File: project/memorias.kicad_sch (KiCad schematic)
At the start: 24 parts, among them U5 M93C66, U6 ICE40HX4K-TQ144, U7 W25X40CLSN

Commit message: Guardado previo, FTDI casi listo
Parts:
- renumbered C20 to C21, C21 to C22, C22 to C23, C23 to C24, C24 to C25
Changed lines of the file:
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@@
 		(on_board yes)
 		(dnp no)
-		(property "Reference" "#PWR038"
+		(property "Reference" "#PWR040"
 			(at 138.43 152.4 0)
 			(effects
@@
 			(project "fpga-utn"
 				(path "/fadb8841-cd7a-4174-937d-7c393e857c90/ddcff421-4d86-4360-8de5-a56571f2fa29"
-					(reference "#PWR038")
+					(reference "#PWR040")
 					(unit 1)
 				)
@@
 		(dnp no)
 		(fields_autoplaced yes)
-		(property "Reference" "#PWR027"
+		(property "Reference" "#PWR029"
 			(at 128.27 67.31 0)
 			(effects
@@
 			(project "fpga-utn"
 				(path "/fadb8841-cd7a-4174-937d-7c393e857c90/ddcff421-4d86-4360-8de5-a56571f2fa29"
-					(reference "#PWR027")
+					(reference "#PWR029")
 					(unit 1)
 				)
@@
 		(on_board yes)
 		(dnp no)
-		(property "Reference" "#PWR029"
+		(property "Reference" "#PWR031"
 			(at 162.56 100.33 0)
 			(effects
@@
 			(project "fpga-utn"
 				(path "/fadb8841-cd7a-4174-937d-7c393e857c90/ddcff421-4d86-4360-8de5-a56571f2fa29"
-					(reference "#PWR029")
+					(reference "#PWR031")
 					(unit 1)
 				)
@@
 		(on_board yes)
 		(dnp no)
-		(property "Reference" "C23"
+		(property "Reference" "C24"
 			(at 144.272 133.858 0)
 			(effects
@@
 			(project "fpga-utn"
 				(path "/fadb8841-cd7a-4174-937d-7c393e857c90/ddcff421-4d86-4360-8de5-a56571f2fa29"
-					(reference "C23")
+					(reference "C24")
 					(unit 1)
 				)
@@
 		(on_board yes)
 		(dnp no)
-		(property "Reference" "#PWR024"
+		(property "Reference" "#PWR026"
 			(at 115.57 55.88 0)
 			(effects
@@
 			(project "fpga-utn"
 				(path "/fadb8841-cd7a-4174-937d-7c393e857c90/ddcff421-4d86-4360-8de5-a56571f2fa29"
-					(reference "#PWR024")
+					(reference "#PWR026")
 					(unit 1)
 				)
@@
 		(on_board yes)
 		(dnp no)
-		(property "Reference" "C20"
+		(property "Reference" "C21"
 			(at 160.782 48.768 0)
 			(effects
@@
 			(project "fpga-utn"
 				(path "/fadb8841-cd7a-4174-937d-7c393e857c90/ddcff421-4d86-4360-8de5-a56571f2fa29"
-					(reference "C20")
+					(reference "C21")
 					(unit 1)
 				)
@@
 		(on_board yes)
 		(dnp no)
-		(property "Reference" "#PWR023"
+		(property "Reference" "#PWR025"
 			(at 160.02 49.53 0)
 			(effects
@@
 			(project "fpga-utn"
 				(path "/fadb8841-cd7a-4174-937d-7c393e857c90/ddcff421-4d86-4360-8de5-a56571f2fa29"
-					(reference "#PWR023")
+					(reference "#PWR025")
 					(unit 1)
 				)
@@
 		(on_board yes)
 		(dnp no)
-		(property "Reference" "C24"
+		(property "Reference" "C25"
 			(at 150.622 133.858 0)
 			(effects
@@
 			(project "fpga-utn"
 				(path "/fadb8841-cd7a-4174-937d-7c393e857c90/ddcff421-4d86-4360-8de5-a56571f2fa29"
-					(reference "C24")
+					(reference "C25")
 					(unit 1)
 				)
@@
 		(on_board yes)
 		(dnp no)
-		(property "Reference" "C21"
+		(property "Reference" "C22"
 			(at 198.882 117.348 0)
 			(effects
@@
 			(project "fpga-utn"
 				(path "/fadb8841-cd7a-4174-937d-7c393e857c90/ddcff421-4d86-4360-8de5-a56571f2fa29"
-					(reference "C21")
+					(reference "C22")
 					(unit 1)
 				)
@@
 		(on_board yes)
 		(dnp no)
-		(property "Reference" "#PWR022"
+		(property "Reference" "#PWR024"
 			(at 128.27 46.99 0)
 			(effects
@@
 			(project "fpga-utn"
 				(path "/fadb8841-cd7a-4174-937d-7c393e857c90/ddcff421-4d86-4360-8de5-a56571f2fa29"
-					(reference "#PWR022")
+					(reference "#PWR024")
 					(unit 1)
 				)
@@
 		(on_board yes)
 		(dnp no)
-		(property "Reference" "C22"
+		(property "Reference" "C23"
 			(at 206.502 117.348 0)
 			(effects
@@
 			(project "fpga-utn"
 				(path "/fadb8841-cd7a-4174-937d-7c393e857c90/ddcff421-4d86-4360-8de5-a56571f2fa29"
-					(reference "C22")
+					(reference "C23")
 					(unit 1)
 				)
@@
 		(dnp no)
 		(fields_autoplaced yes)
-		(property "Reference" "#PWR026"
+		(property "Reference" "#PWR028"
 			(at 160.02 62.23 0)
 			(effects
@@
 			(project "fpga-utn"
 				(path "/fadb8841-cd7a-4174-937d-7c393e857c90/ddcff421-4d86-4360-8de5-a56571f2fa29"
-					(reference "#PWR026")
+					(reference "#PWR028")
 					(unit 1)
 				)
@@
 		(on_board yes)
 		(dnp no)
-		(property "Reference" "#PWR025"
+		(property "Reference" "#PWR027"
 			(at 151.13 59.69 0)
 			(effects
@@
 			(project "fpga-utn"
 				(path "/fadb8841-cd7a-4174-937d-7c393e857c90/ddcff421-4d86-4360-8de5-a56571f2fa29"
-					(reference "#PWR025")
+					(reference "#PWR027")
 					(unit 1)
 				)
@@
 		(on_board yes)
 		(dnp no)
-		(property "Reference" "#PWR032"
+		(property "Reference" "#PWR034"
 			(at 198.12 119.38 0)
 			(effects
@@
 			(project "fpga-utn"
 				(path "/fadb8841-cd7a-4174-937d-7c393e857c90/ddcff421-4d86-4360-8de5-a56571f2fa29"
-					(reference "#PWR032")
+					(reference "#PWR034")
 					(unit 1)
 				)
@@
 		(on_board yes)
 		(dnp no)
-		(property "Reference" "#PWR033"
+		(property "Reference" "#PWR035"
 			(at 205.74 129.54 0)
 			(effects
@@
 			(project "fpga-utn"
 				(path "/fadb8841-cd7a-4174-937d-7c393e857c90/ddcff421-4d86-4360-8de5-a56571f2fa29"
-					(reference "#PWR033")
+					(reference "#PWR035")
 					(unit 1)
 				)
@@
 		(on_board yes)
 		(dnp no)
-		(property "Reference" "#PWR031"
+		(property "Reference" "#PWR033"
 			(at 180.34 106.68 0)
 			(effects
@@
 			(project "fpga-utn"
 				(path "/fadb8841-cd7a-4174-937d-7c393e857c90/ddcff421-4d86-4360-8de5-a56571f2fa29"
-					(reference "#PWR031")
+					(reference "#PWR033")
 					(unit 1)
 				)
@@
 		(on_board yes)
 		(dnp no)
-		(property "Reference" "#PWR036"
+		(property "Reference" "#PWR038"
 			(at 115.57 144.78 0)
 			(effects
@@
 			(project "fpga-utn"
 				(path "/fadb8841-cd7a-4174-937d-7c393e857c90/ddcff421-4d86-4360-8de5-a56571f2fa29"
-					(reference "#PWR036")
+					(reference "#PWR038")
 					(unit 1)
 				)
@@
 		(on_board yes)
 		(dnp no)
-		(property "Reference" "#PWR030"
+		(property "Reference" "#PWR032"
 			(at 127 104.14 0)
 			(effects
@@
 			(project "fpga-utn"
 				(path "/fadb8841-cd7a-4174-937d-7c393e857c90/ddcff421-4d86-4360-8de5-a56571f2fa29"
-					(reference "#PWR030")
+					(reference "#PWR032")
 					(unit 1)
 				)
@@
 		(dnp no)
 		(fields_autoplaced yes)
-		(property "Reference" "#PWR035"
+		(property "Reference" "#PWR037"
 			(at 180.34 139.7 0)
 			(effects
@@
 			(project "fpga-utn"
 				(path "/fadb8841-cd7a-4174-937d-7c393e857c90/ddcff421-4d86-4360-8de5-a56571f2fa29"
-					(reference "#PWR035")
+					(reference "#PWR037")
 					(unit 1)
 				)
@@
 		(dnp no)
 		(fields_autoplaced yes)
-		(property "Reference" "#PWR037"
+		(property "Reference" "#PWR039"
 			(at 149.86 147.32 0)
 			(effects
@@
 			(project "fpga-utn"
 				(path "/fadb8841-cd7a-4174-937d-7c393e857c90/ddcff421-4d86-4360-8de5-a56571f2fa29"
-					(reference "#PWR037")
+					(reference "#PWR039")
 					(unit 1)
 				)
@@
 		(on_board yes)
 		(dnp no)
-		(property "Reference" "#PWR028"
+		(property "Reference" "#PWR030"
 			(at 137.16 92.71 0)
 			(effects
@@
 			(project "fpga-utn"
 				(path "/fadb8841-cd7a-4174-937d-7c393e857c90/ddcff421-4d86-4360-8de5-a56571f2fa29"
-					(reference "#PWR028")
+					(reference "#PWR030")
 					(unit 1)
 				)
@@
 		(on_board yes)
 		(dnp no)
-		(property "Reference" "#PWR034"
+		(property "Reference" "#PWR036"
 			(at 154.94 130.81 0)
 			(effects
@@
 			(project "fpga-utn"
 				(path "/fadb8841-cd7a-4174-937d-7c393e857c90/ddcff421-4d86-4360-8de5-a56571f2fa29"
-					(reference "#PWR034")
-					(unit 1)
-				)
+					(reference "#PWR036")
+					(unit 1)
+				)

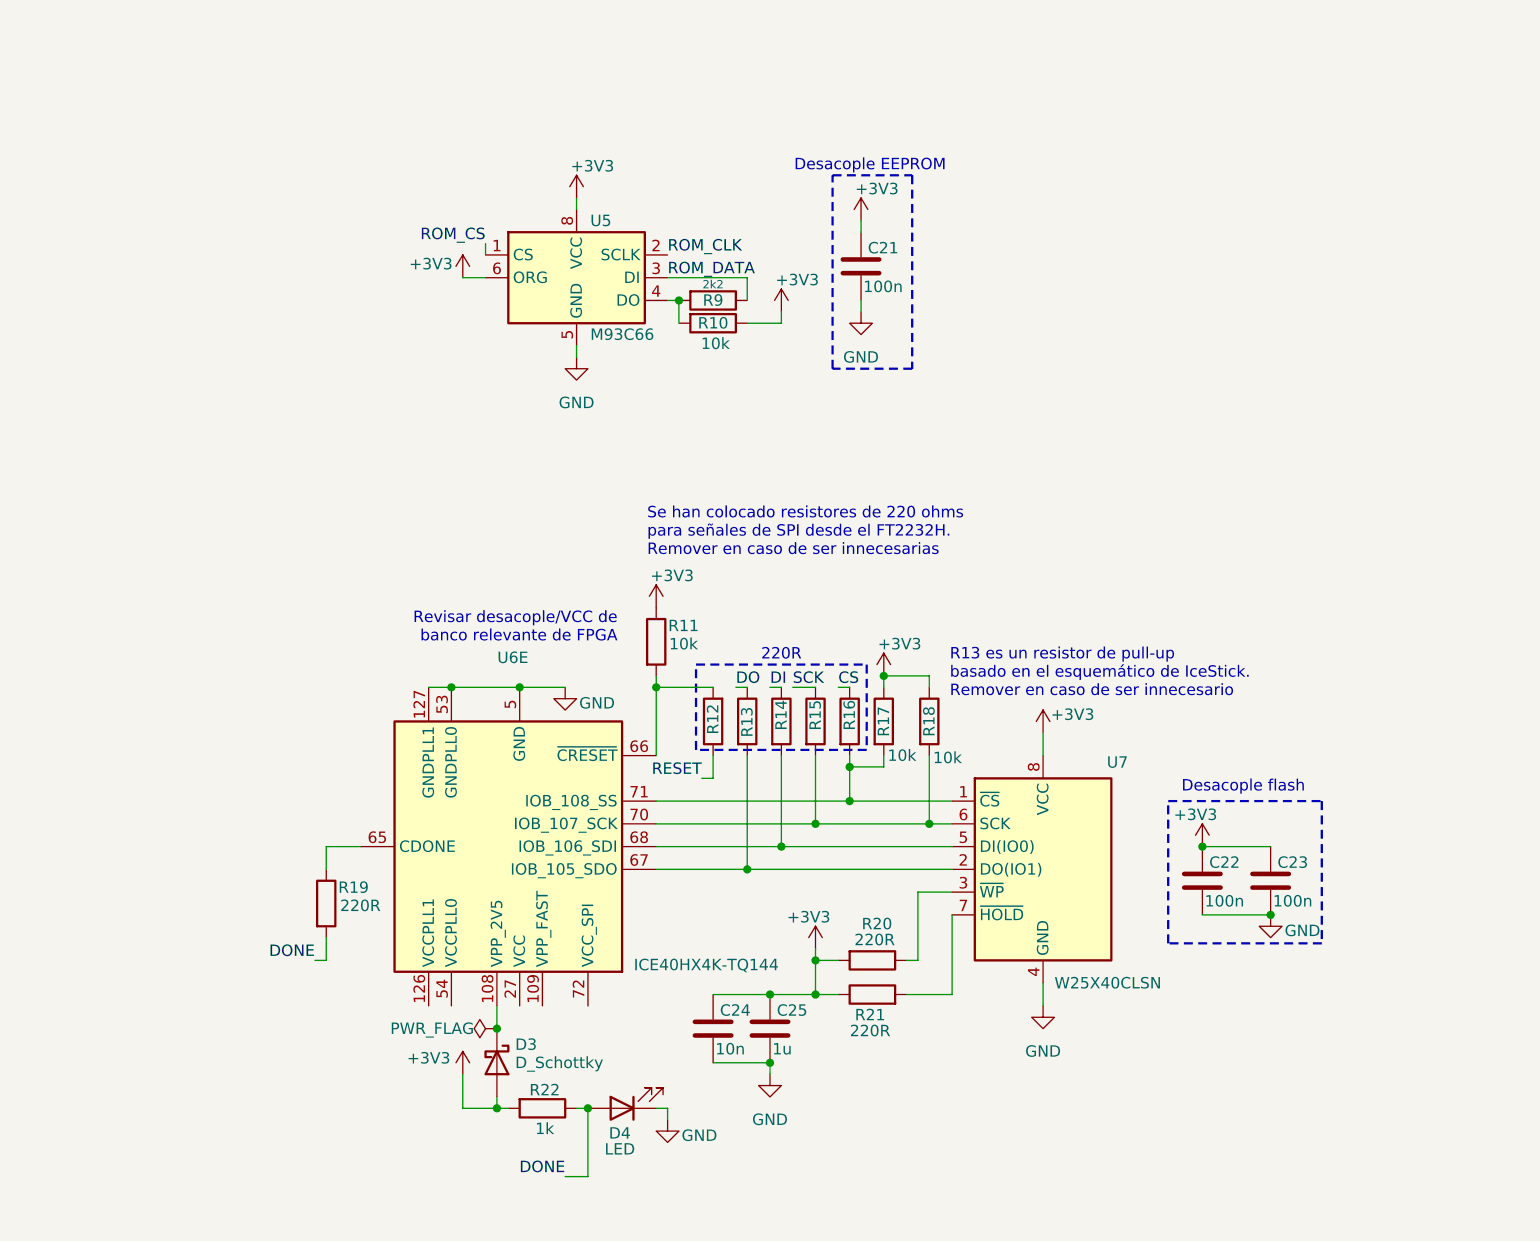
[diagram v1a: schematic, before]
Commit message: Corrigiendo errores de conexiones en la memorias
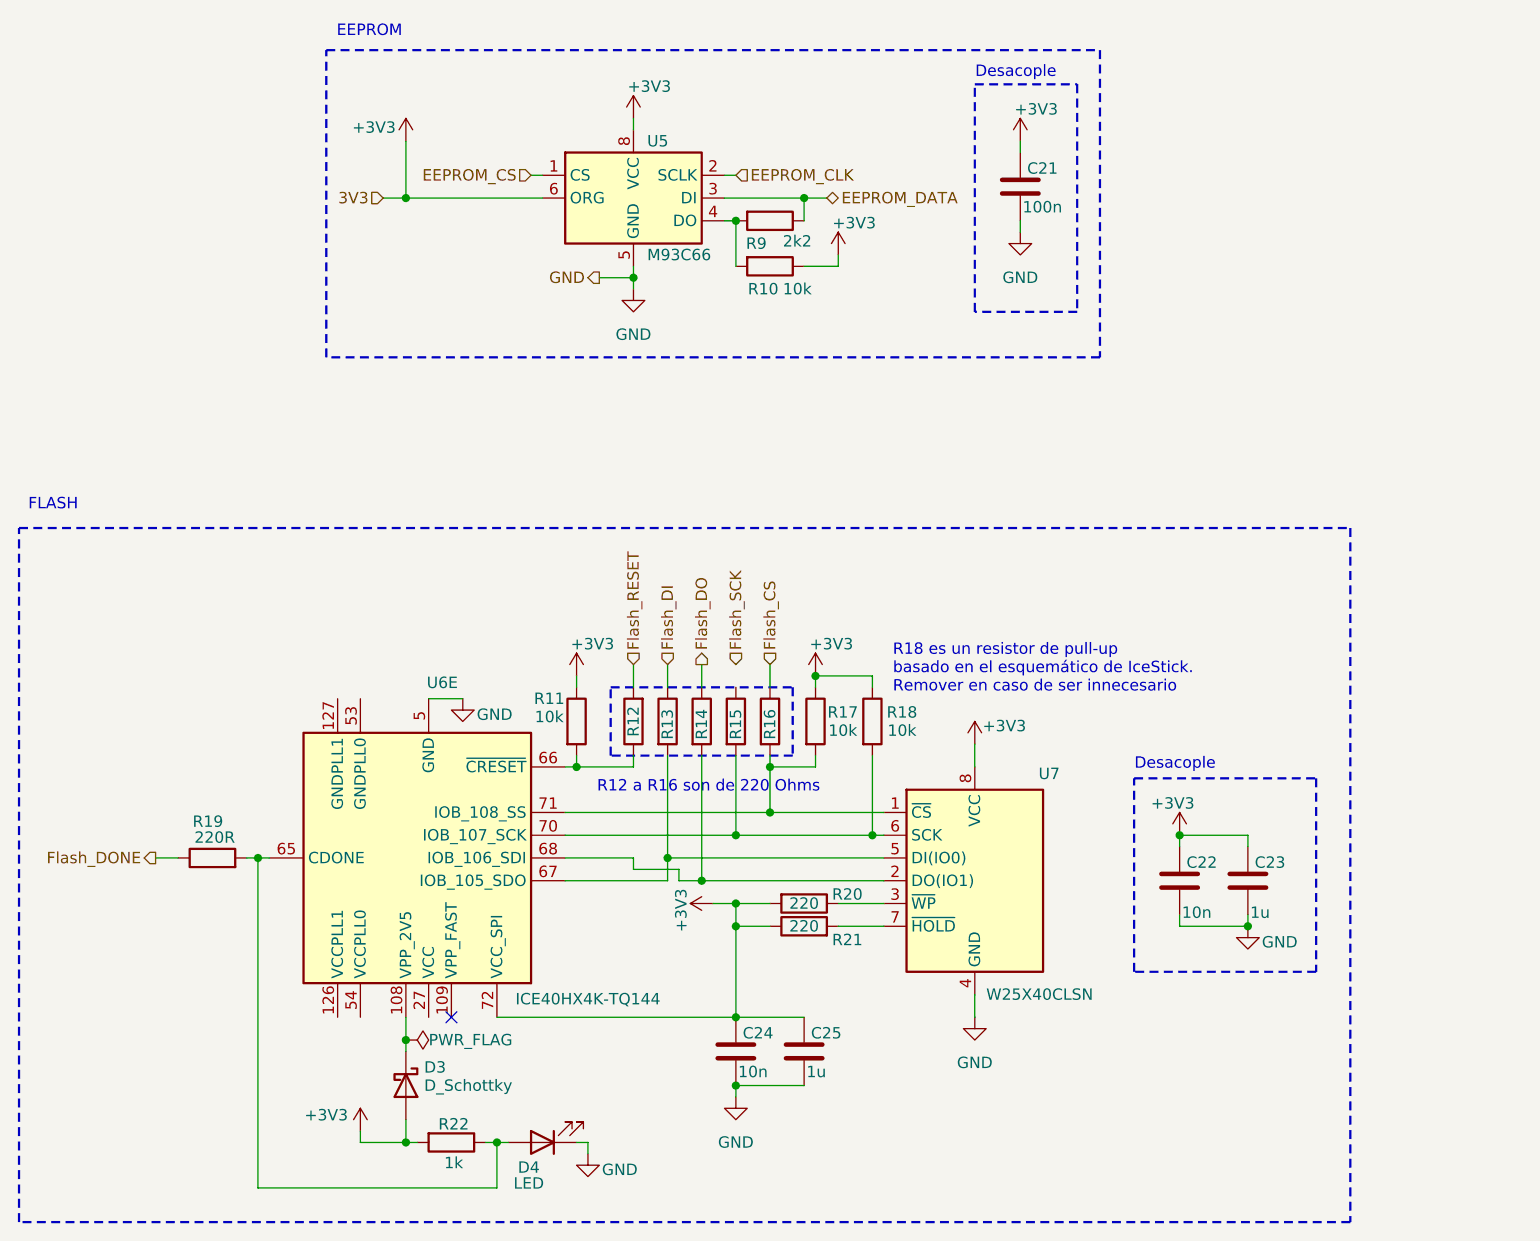
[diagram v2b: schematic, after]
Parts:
- C22: value 100n -> 10n
- C23: value 100n -> 1u
- R12, R20, R21: value 220R -> 220
- renumbered R14 to R13, R13 to R14
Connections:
- net DONE is gone; now on an unnamed net: D4.2 (A), R19.2, R22.1
- net RESET is gone; now on an unnamed net: R12.1
- net +3V3: now also U6.72 (VCC_SPI)
- net GND: no longer U6.127 (GNDPLL1), U6.53 (GNDPLL0)
- net at U6.65 (CDONE): no longer R19.1
- net at R13.2, U7.5 (DI(IO0)): now also U6.67 (IOB_105_SDO); no longer U6.68 (IOB_106_SDI)
- net at R11.2, U6.66 (~{CRESET}): no longer R12.2
- net at R14.2, U7.2 (DO(IO1)): now also U6.68 (IOB_106_SDI); no longer U6.67 (IOB_105_SDO)
- net CS renamed Flash_CS
- net DI renamed Flash_DI
- net DO renamed Flash_DO
- net ROM_CLK renamed EEPROM_CLK
- net ROM_CS renamed EEPROM_CS
- net ROM_DATA renamed EEPROM_DATA
- net SCK: no longer names the net of R15.1
- new net Flash_DONE: R19.1
- new net Flash_RESET: R12.2
- no-connect marks 0 -> 1
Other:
- note added: "Desacople"
- note added: "EEPROM"
- note added: "FLASH"
- note added: "R12 a R16 son de 220 Ohms"
- note added: "R18 es un resistor de pull-up basado en el esquemático de IceStick. Remover en caso de ser innecesario"
- note removed: "220R"
- note removed: "Desacople EEPROM"
- note removed: "Desacople flash"
- note removed: "R13 es un resistor de pull-up basado en el esquemático de IceStick. Remover en caso de ser innecesario"
- note removed: "Revisar desacople/VCC de banco relevante de FPGA"
- note removed: "Se han colocado resistores de 220 ohms para señales de SPI desde el FT2232H. Remover en caso de ser innecesarias"
- moved on the sheet: C21, C22, C23, C24, C25, D3, D4, R10, R11, R12, R13, R14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

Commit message: Inicio de la PCB y conexion del PLL
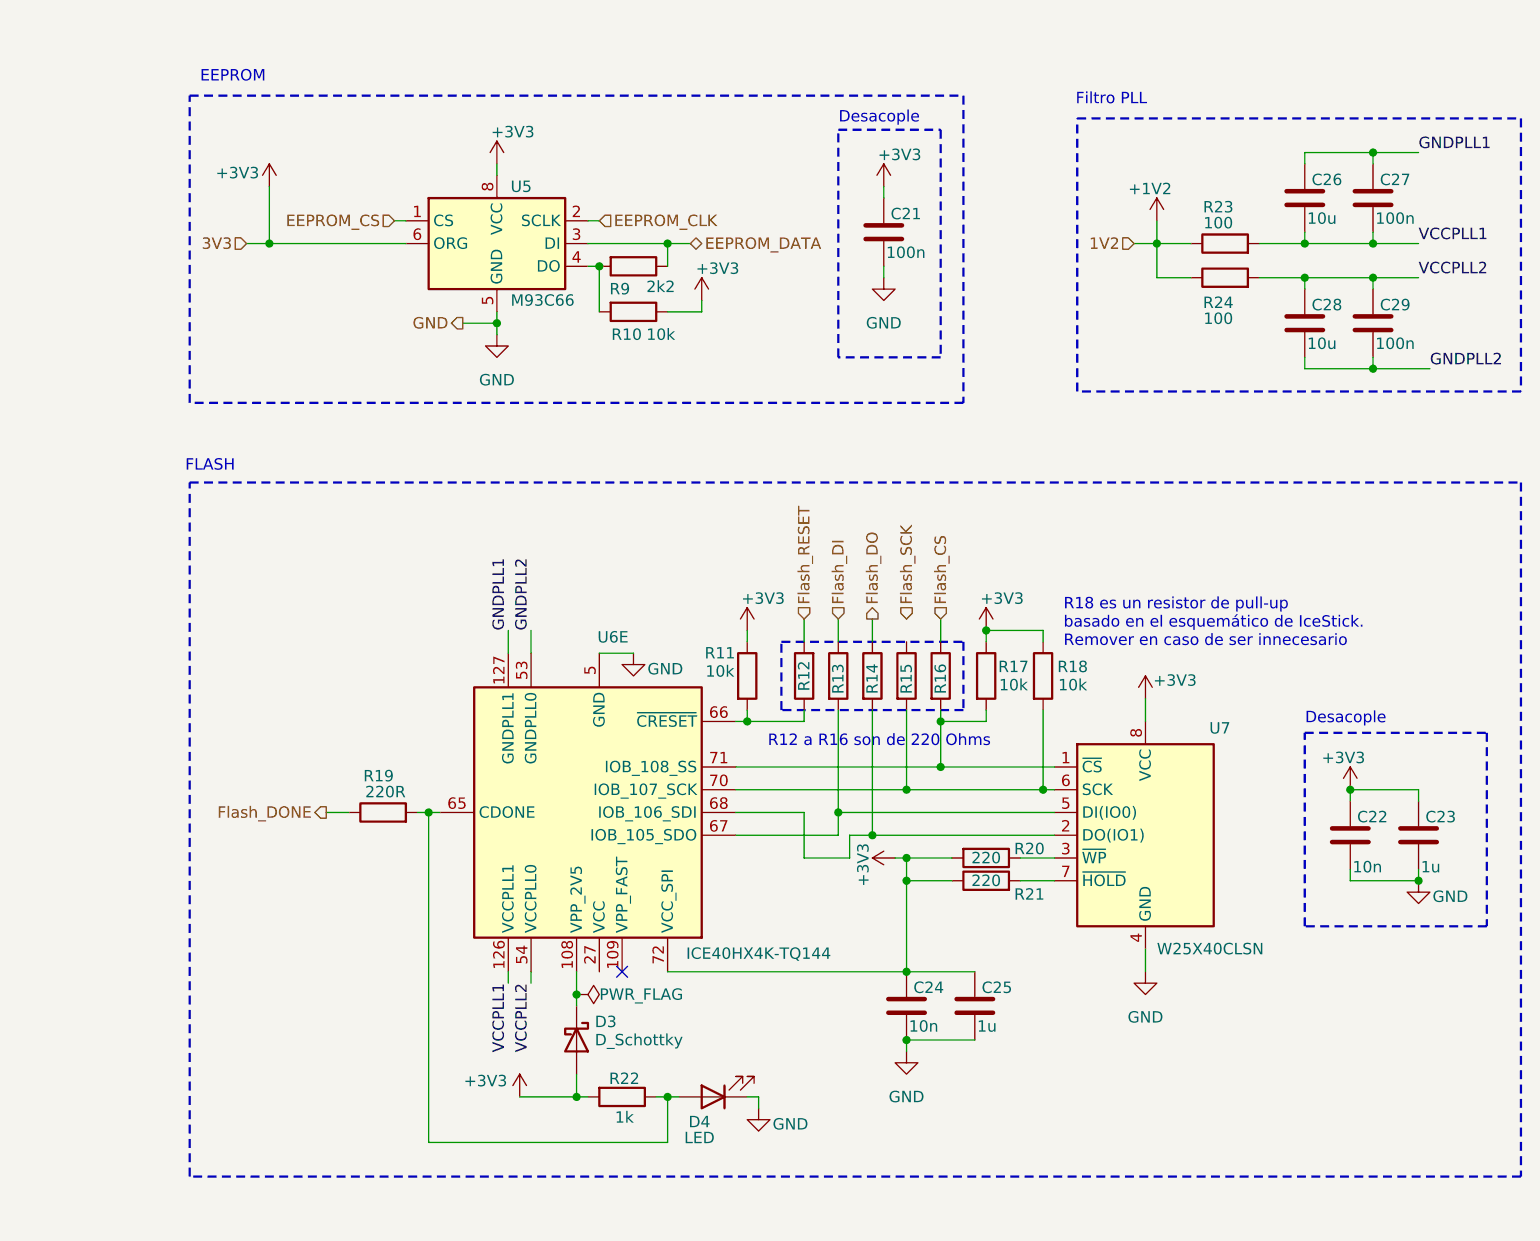
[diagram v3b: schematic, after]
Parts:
- added C26, C28: 10u, Capacitor_SMD:C_1206_3216Metric, symbol Device:C
- added C27, C29: 100n, Capacitor_SMD:C_1206_3216Metric, symbol Device:C
- added R23, R24: 100, Resistor_SMD:R_1206_3216Metric, symbol Device:R
- C21, C22, C23, C24, C25: footprint (none) -> Capacitor_SMD:C_1206_3216Metric
- D3: footprint (none) -> Diode_SMD:D_1206_3216Metric
- D4: footprint (none) -> libraries:WL-SMTW_3528
- R10, R11, R12, R13, R14, R15, R16, R17, R18, R19, R20, R21, R22, R9: footprint (none) -> Resistor_SMD:R_1206_3216Metric
- U5: footprint (none) -> Package_SO:SOIC-8_3.9x4.9mm_P1.27mm
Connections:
- net VCCPLL1: now reaches U6.126 (VCCPLL1)
- net VCCPLL1: now also C26.2, C27.2, R23.2
- net GNDPLL1: now reaches U6.127 (GNDPLL1)
- net GNDPLL1: now also C26.1, C27.1
- net GNDPLL2: now reaches U6.53 (GNDPLL0)
- net GNDPLL2: now also C28.2, C29.2
- net VCCPLL2: now reaches U6.54 (VCCPLL0)
- net VCCPLL2: now also C28.1, C29.1, R24.2
- new net +1V2: R23.1, R24.1
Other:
- note added: "Filtro PLL"
- moved on the sheet: C21, C22, C23, C24, C25, D3, D4, R10, R11, R12, R13, R14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
